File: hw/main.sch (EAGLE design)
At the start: 40 parts, among them Q1 732-MC14632.76KA-A0R, T1 863-MMBT4401LT1G, T2 863-MMBT4401LT1G, T3 863-MMBT4401LT1G, U1 579-MCP1703T-3002ECB, U2 638-CLS1522CL213RTR8, U3 595-MSP430G2553IPW28, U4 638-CLS1522CL213RTR8, X1 798-DF134P125H51, X2 798-DF134P125H51

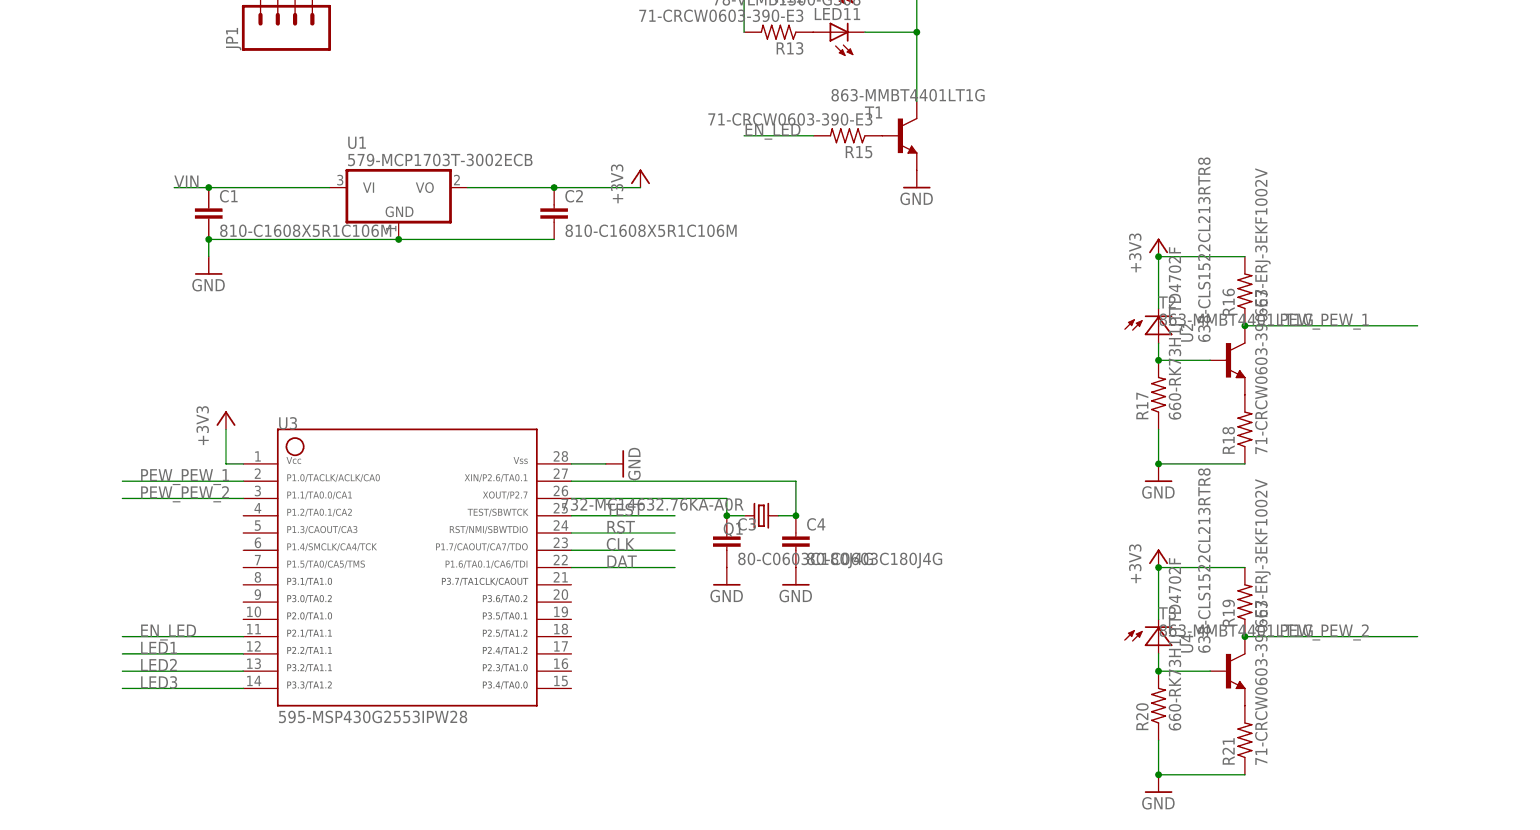
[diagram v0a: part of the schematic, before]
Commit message: Remove transistor and switch laser input to ADC polling.
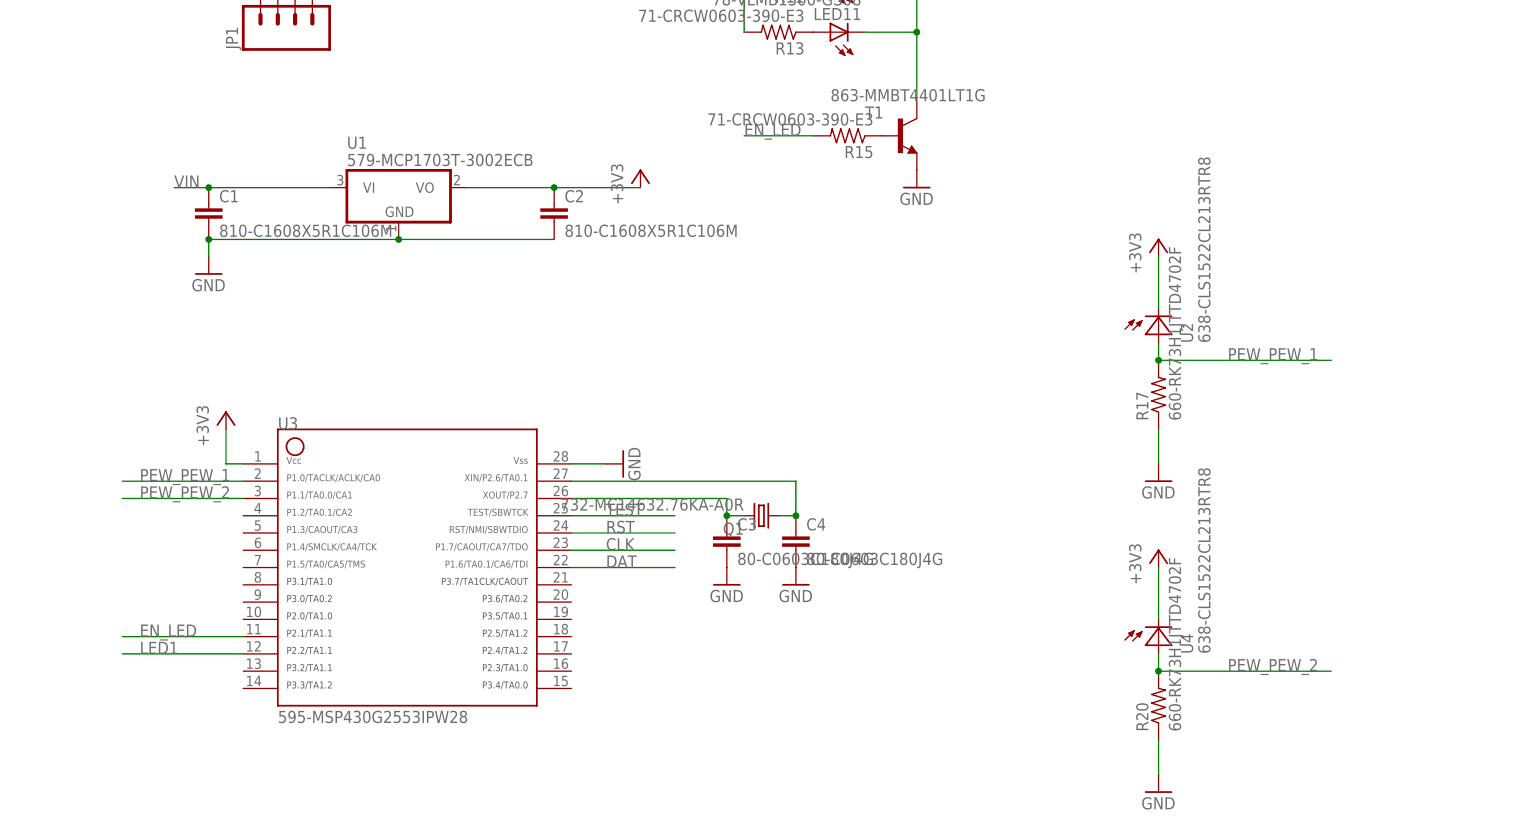
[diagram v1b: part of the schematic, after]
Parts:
- removed R16, R19: 667-ERJ-3EKF1002V, rcl:R-US_R0603
- removed R18, R21: 71-CRCW0603-390-E3, rcl:R-US_R0603
- removed T2, T3: 863-MMBT4401LT1G, transistor:MMBT4401LT1-NPN-SOT23-BEC
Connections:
- removed net 1: R20.2, T3.B, U4.A
- removed net 121231: R17.2, T2.B, U2.A
- removed net LED2: U3.13
- removed net LED3: U3.14
- removed net N$2: R18.2, T2.E
- removed net N$3: R21.2, T3.E
- net +3V3: no longer R16.2, R19.2
- net GND: no longer R18.1, R21.1
- net PEW_PEW_1: now also R17.2, U2.A; no longer R16.1, T2.C
- net PEW_PEW_2: now also R20.2, U4.A; no longer R19.1, T3.C
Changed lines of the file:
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@@
 <?xml version="1.0" encoding="utf-8"?>
 <!DOCTYPE eagle SYSTEM "eagle.dtd">
-<eagle version="6.0">
+<eagle version="6.1">
 <drawing>
 <settings>
@@
 <setting verticaltext="up"/>
 </settings>
-<grid distance="0.1" unitdist="inch" unit="inch" style="lines" multiple="1" display="no" altdistance="0.01" altunitdist="inch" altunit="inch"/>
+<grid distance="0.1" unitdist="inch" unit="inch" style="lines" multiple="1" display="yes" altdistance="0.01" altunitdist="inch" altunit="inch"/>
 <layers>
 <layer number="1" name="Top" color="4" fill="1" visible="no" active="no"/>
@@
 <part name="+3V3" library="supply1" deviceset="+3V3" device=""/>
 <part name="GND5" library="supply1" deviceset="GND" device=""/>
-<part name="T2" library="transistor" deviceset="*-NPN-" device="SOT23-BEC" technology="MMBT4401LT1" value="863-MMBT4401LT1G"/>
-<part name="R16" library="rcl" deviceset="R-US_" device="R0603" value="667-ERJ-3EKF1002V"/>
-<part name="R18" library="rcl" deviceset="R-US_" device="R0603" value="71-CRCW0603-390-E3"/>
 <part name="LED5" library="SparkFun-LED" deviceset="LED" device="0603" value="78-VLMB1300-GS08"/>
 <part name="LED3" library="SparkFun-LED" deviceset="LED" device="0603" value="78-VLMB1300-GS08"/>
@@
 <part name="+3V5" library="supply1" deviceset="+3V3" device=""/>
 <part name="GND6" library="supply1" deviceset="GND" device=""/>
-<part name="T3" library="transistor" deviceset="*-NPN-" device="SOT23-BEC" technology="MMBT4401LT1" value="863-MMBT4401LT1G"/>
-<part name="R19" library="rcl" deviceset="R-US_" device="R0603" value="667-ERJ-3EKF1002V"/>
-<part name="R21" library="rcl" deviceset="R-US_" device="R0603" value="71-CRCW0603-390-E3"/>
 <part name="LED11" library="SparkFun-LED" deviceset="LED" device="0603" value="78-VLMB1300-GS08"/>
 <part name="LED9" library="SparkFun-LED" deviceset="LED" device="0603" value="78-VLMB1300-GS08"/>
@@
 <instance part="+3V3" gate="G$1" x="142.24" y="71.12"/>
 <instance part="GND5" gate="1" x="142.24" y="35.56"/>
-<instance part="T2" gate="G$1" x="152.4" y="53.34"/>
-<instance part="R16" gate="G$1" x="154.94" y="63.5" rot="R90"/>
-<instance part="R18" gate="G$1" x="154.94" y="43.18" rot="R90"/>
 <instance part="LED5" gate="G$1" x="93.98" y="124.46" rot="R90"/>
 <instance part="LED3" gate="G$1" x="93.98" y="132.08" rot="R90"/>
@@
 <instance part="+3V5" gate="G$1" x="142.24" y="25.4"/>
 <instance part="GND6" gate="1" x="142.24" y="-10.16"/>
-<instance part="T3" gate="G$1" x="152.4" y="7.62"/>
-<instance part="R19" gate="G$1" x="154.94" y="17.78" rot="R90"/>
-<instance part="R21" gate="G$1" x="154.94" y="-2.54" rot="R90"/>
 <instance part="LED11" gate="G$1" x="93.98" y="101.6" rot="R90"/>
 <instance part="LED9" gate="G$1" x="93.98" y="109.22" rot="R90"/>
@@
 <pinref part="GND5" gate="1" pin="GND"/>
 <wire x1="142.24" y1="38.1" x2="142.24" y2="43.18" width="0.1524" layer="91"/>
-<pinref part="R18" gate="G$1" pin="1"/>
-<wire x1="142.24" y1="38.1" x2="154.94" y2="38.1" width="0.1524" layer="91"/>
-<junction x="142.24" y="38.1"/>
 </segment>
 <segment>
@@
 <pinref part="GND6" gate="1" pin="GND"/>
 <wire x1="142.24" y1="-7.62" x2="142.24" y2="-2.54" width="0.1524" layer="91"/>
-<pinref part="R21" gate="G$1" pin="1"/>
-<wire x1="142.24" y1="-7.62" x2="154.94" y2="-7.62" width="0.1524" layer="91"/>
-<junction x="142.24" y="-7.62"/>
 </segment>
 <segment>
@@
 </segment>
 </net>
-<net name="121231" class="0">
-<segment>
-<pinref part="U2" gate="G$1" pin="A"/>
-<pinref part="R17" gate="G$1" pin="2"/>
-<wire x1="142.24" y1="55.88" x2="142.24" y2="53.34" width="0.1524" layer="91"/>
-<wire x1="142.24" y1="53.34" x2="149.86" y2="53.34" width="0.1524" layer="91"/>
-<pinref part="T2" gate="G$1" pin="B"/>
-<junction x="142.24" y="53.34"/>
-</segment>
-</net>
 <net name="+3V3" class="0">
 <segment>
@@
 <wire x1="142.24" y1="60.96" x2="142.24" y2="68.58" width="0.1524" layer="91"/>
 <pinref part="+3V3" gate="G$1" pin="+3V3"/>
-<pinref part="R16" gate="G$1" pin="2"/>
-<wire x1="142.24" y1="68.58" x2="154.94" y2="68.58" width="0.1524" layer="91"/>
-<junction x="142.24" y="68.58"/>
 </segment>
 <segment>
@@
 <wire x1="142.24" y1="15.24" x2="142.24" y2="22.86" width="0.1524" layer="91"/>
 <pinref part="+3V5" gate="G$1" pin="+3V3"/>
-<pinref part="R19" gate="G$1" pin="2"/>
-<wire x1="142.24" y1="22.86" x2="154.94" y2="22.86" width="0.1524" layer="91"/>
-<junction x="142.24" y="22.86"/>
 </segment>
 <segment>
@@
 <net name="PEW_PEW_2" class="0">
 <segment>
-<pinref part="R19" gate="G$1" pin="1"/>
-<pinref part="T3" gate="G$1" pin="C"/>
-<wire x1="154.94" y1="12.7" x2="180.34" y2="12.7" width="0.1524" layer="91"/>
-<label x="160.02" y="12.7" size="1.778" layer="95"/>
-<junction x="154.94" y="12.7"/>
+<wire x1="142.24" y1="7.62" x2="167.64" y2="7.62" width="0.1524" layer="91"/>
+<label x="152.4" y="7.62" size="1.778" layer="95"/>
+<pinref part="U4" gate="G$1" pin="A"/>
+<pinref part="R20" gate="G$1" pin="2"/>
+<wire x1="142.24" y1="10.16" x2="142.24" y2="7.62" width="0.1524" layer="91"/>
+<junction x="142.24" y="7.62"/>
 </segment>
 <segment>
@@
 <wire x1="7.62" y1="33.02" x2="-10.16" y2="33.02" width="0.1524" layer="91"/>
 <label x="-7.62" y="33.02" size="1.778" layer="95"/>
-</segment>
-</net>
-<net name="N$2" class="0">
-<segment>
-<pinref part="T2" gate="G$1" pin="E"/>
-<pinref part="R18" gate="G$1" pin="2"/>
 </segment>
 </net>
@@
 <wire x1="256.54" y1="35.56" x2="238.76" y2="35.56" width="0.1524" layer="91"/>
 <label x="248.92" y="35.56" size="1.778" layer="95" rot="MR0"/>
-</segment>
-</net>
-<net name="1" class="0">
-<segment>
-<pinref part="U4" gate="G$1" pin="A"/>
-<pinref part="R20" gate="G$1" pin="2"/>
-<wire x1="142.24" y1="10.16" x2="142.24" y2="7.62" width="0.1524" layer="91"/>
-<wire x1="142.24" y1="7.62" x2="149.86" y2="7.62" width="0.1524" layer="91"/>
-<pinref part="T3" gate="G$1" pin="B"/>
-<junction x="142.24" y="7.62"/>
-</segment>
-</net>
-<net name="N$3" class="0">
-<segment>
-<pinref part="T3" gate="G$1" pin="E"/>
-<pinref part="R21" gate="G$1" pin="2"/>
 </segment>
 </net>
@@
 <net name="PEW_PEW_1" class="0">
 <segment>
-<pinref part="R16" gate="G$1" pin="1"/>
-<pinref part="T2" gate="G$1" pin="C"/>
-<wire x1="154.94" y1="58.42" x2="180.34" y2="58.42" width="0.1524" layer="91"/>
-<label x="160.02" y="58.42" size="1.778" layer="95"/>
-<junction x="154.94" y="58.42"/>
-</segment>
-<segment>
 <pinref part="U3" gate="G$1" pin="2"/>
 <wire x1="7.62" y1="35.56" x2="-10.16" y2="35.56" width="0.1524" layer="91"/>
 <label x="-7.62" y="35.56" size="1.778" layer="95"/>
+</segment>
+<segment>
+<pinref part="U2" gate="G$1" pin="A"/>
+<pinref part="R17" gate="G$1" pin="2"/>
+<wire x1="142.24" y1="55.88" x2="142.24" y2="53.34" width="0.1524" layer="91"/>
+<wire x1="142.24" y1="53.34" x2="167.64" y2="53.34" width="0.1524" layer="91"/>
+<junction x="142.24" y="53.34"/>
+<label x="152.4" y="53.34" size="1.778" layer="95"/>
 </segment>
 </net>
@@
 </segment>
 </net>
-<net name="LED2" class="0">
-<segment>
-<pinref part="U3" gate="G$1" pin="13"/>
-<wire x1="7.62" y1="7.62" x2="-10.16" y2="7.62" width="0.1524" layer="91"/>
-<label x="-7.62" y="7.62" size="1.778" layer="95"/>
-</segment>
-</net>
-<net name="LED3" class="0">
-<segment>
-<pinref part="U3" gate="G$1" pin="14"/>
-<wire x1="7.62" y1="5.08" x2="-10.16" y2="5.08" width="0.1524" layer="91"/>
-<label x="-7.62" y="5.08" size="1.778" layer="95"/>
-</segment>
-</net>

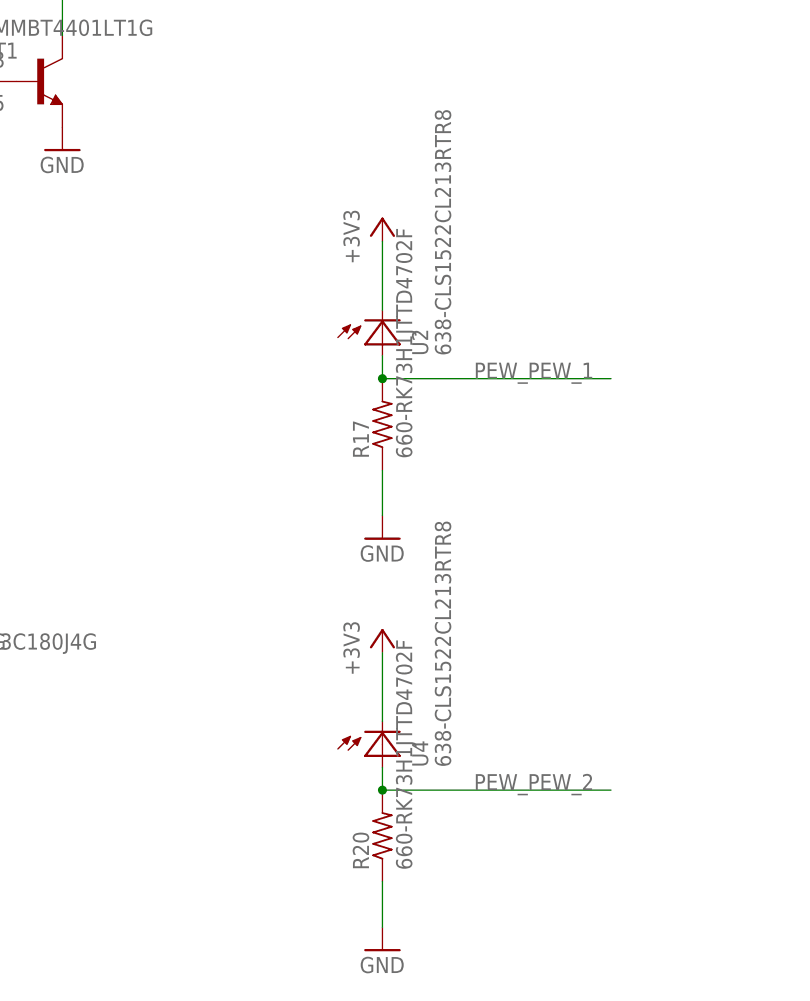
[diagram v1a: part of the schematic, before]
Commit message: Fix resistor value for light detector.
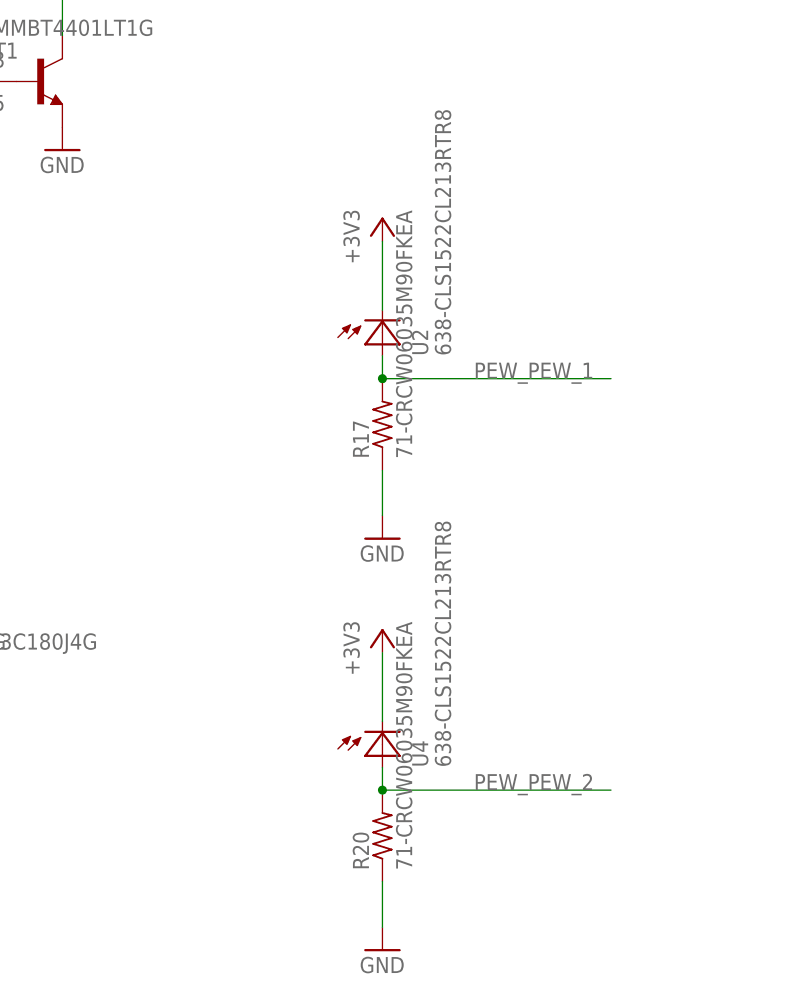
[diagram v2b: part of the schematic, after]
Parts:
- R17, R20: value 660-RK73H1JTTD4702F -> 71-CRCW06035M90FKEA
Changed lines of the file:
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@@
 <setting verticaltext="up"/>
 </settings>
-<grid distance="0.1" unitdist="inch" unit="inch" style="lines" multiple="1" display="yes" altdistance="0.01" altunitdist="inch" altunit="inch"/>
+<grid distance="0.1" unitdist="inch" unit="inch" style="lines" multiple="1" display="no" altdistance="0.01" altunitdist="inch" altunit="inch"/>
 <layers>
 <layer number="1" name="Top" color="4" fill="1" visible="no" active="no"/>
@@
 <part name="GND3" library="supply1" deviceset="GND" device=""/>
 <part name="GND4" library="supply1" deviceset="GND" device=""/>
-<part name="R17" library="rcl" deviceset="R-US_" device="R0603" value="660-RK73H1JTTD4702F"/>
+<part name="R17" library="rcl" deviceset="R-US_" device="R0603" value="71-CRCW06035M90FKEA"/>
 <part name="U1" library="linear" deviceset="MCP1703" device="CB" value="579-MCP1703T-3002ECB"/>
 <part name="+3V1" library="supply1" deviceset="+3V3" device=""/>
@@
 <part name="X1" library="con-molex" deviceset="53?-04" device="261" value="798-DF134P125H51"/>
 <part name="U4" library="torpedo" deviceset="CLS15" device="CLS15" value="638-CLS1522CL213RTR8"/>
-<part name="R20" library="rcl" deviceset="R-US_" device="R0603" value="660-RK73H1JTTD4702F"/>
+<part name="R20" library="rcl" deviceset="R-US_" device="R0603" value="71-CRCW06035M90FKEA"/>
 <part name="+3V5" library="supply1" deviceset="+3V3" device=""/>
 <part name="GND6" library="supply1" deviceset="GND" device=""/>

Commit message: Updated target to simplify circuit and make immune to spurious light sources.
The design has been reduced in size from ~40mm diameter to ~21mm diameter. The sensor was changed from a single-color (red) detector to a full-spectrum + white sensor since the old version would get tripped by white light (and camera flashes). The microcontroller was changed from the MSP430G2553 to the MSP430G2452 in the 14 pin package to save space. The new target will mount from the bottom and sit in the bottom of the table tennis ball instead of in the middle.
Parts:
- removed C3, C4: 80-C0603C180J4G, SparkFun-Passives:CAP0603-CAP
- removed LED1, LED11, LED3, LED5, LED7, LED9: 78-VLMB1300-GS08, SparkFun-LED:LED0603
- removed LED2, LED4: 720-LGQ971-KN-1, SparkFun-LED:LED0603
- removed Q1: 732-MC14632.76KA-A0R, SparkFun:CRYSTALEPSONMC146
- removed R11, R13, R15, R9: 71-CRCW0603-390-E3, rcl:R-US_R0603
- removed R17, R20: 71-CRCW06035M90FKEA, rcl:R-US_R0603
- removed U4: 638-CLS1522CL213RTR8, torpedo:CLS15CLS15
- added D1, D2: VLMB1300-GS08, SparkFun-LED:LED0603
- added D3, D4: VLMS1300-GS08, SparkFun-LED:LED0603
- added R8: CRCW0603200RFKEA, rcl:R-US_R0603
- added T2: PMBT4401,215, transistor:MMBT4401LT1-NPN-SOT23-BEC
- C1, C2: value 810-C1608X5R1C106M -> C1608X5R1C106M080AB
- JP1: device SparkFun:M04PTH -> SparkFun-Connectors:M03PTH
- R1, R2: value 71-CRCW0603-390-E3 -> RK73H1JTTD4702F
- R3, R6: value 660-RK73H1JTTD4702F -> CRCW0603200RFKEA
- R4, R5, R7: value 71-CRCW0603-390-E3 -> CRCW0603200RFKEA
- T1: value 863-MMBT4401LT1G -> PMBT4401,215
- U1: value 579-MCP1703T-3002ECB -> MCP1703T-3002E/CB
- U2: value 638-CLS1522CL213RTR8 -> MSP430G2452IPW14R; device torpedo:CLS15CLS15 -> TI_MSP430_v16:G2X[1/5]2---PW14
- U3: value 595-MSP430G2553IPW28 -> TCS3414CS; device torpedo:MSP430G2553 -> torpedo:TCS3414CS
- X1, X2: value 798-DF134P125H51 -> DF13-4P-1.25V(50); device con-molex:53261-04 -> con-molex:53398-04
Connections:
- removed net EN_LED: R15.2, U3.11
- removed net LED1: LED2.C, LED4.C, U3.12
- removed net N$11: LED7.A, R9.1
- removed net N$12: C4.1, Q1.1, U3.27
- removed net N$13: C3.1, Q1.2, U3.26
- removed net N$5: LED1.A, R1.1
- removed net N$9: LED4.A, R5.1
- removed net PEW_PEW_1: R17.2, U2.A, U3.2
- removed net PEW_PEW_2: R20.2, U3.3, U4.A
- new net BLUE_LED: R5.2, U2.5
- new net CNT: U2.2, X1-4.S, X2-4.S
- new net INT: U2.7, U3.INT
- new net N$2: D3.C, D4.C, T2.C
- new net RED_LED: R8.2, U2.4
- new net SET: U2.3, X1-3.S, X2-3.S
- new net SYNC: U2.6, U3.SYNC
- net +3V3: now also R6.2, U2.1, U3.VCC; no longer JP1.4, R11.2, R13.2, R2.2, R5.2, R9.2, U2.C, U3.1, U4.C
- net CLK: now also U2.8, U3.SCL; no longer U3.23, X1-3.S, X2-3.S
- net DAT: now also U2.9, U3.SDA; no longer U3.22, X1-4.S, X2-4.S
- net GND: now also R2.1, T2.E, U2.14, U3.GND; no longer C3.2, C4.2, R17.1, R20.1, R6.1, U3.28
- net LED: now also D1.C, D2.C; no longer LED1.C, LED11.C, LED3.C, LED5.C, LED7.C, LED9.C
- net N$1: now also D4.A; no longer LED5.A
- net N$10: now also D3.A, R6.1; no longer LED2.A, R2.1
- net N$18: now also R5.1; no longer R15.1
- net N$4: now also R8.1, T2.B; no longer LED3.A, R4.1
- net N$6: now also D2.A, R4.1; no longer LED11.A, R13.1
- net N$7: now also D1.A, R3.1; no longer LED9.A, R11.1
- net RST: now also JP1.2, R2.2, U2.10; no longer JP1.1, R3.1, U3.24
- net TEST: now also JP1.1, R1.1, U2.11; no longer JP1.2, R6.2, U3.25
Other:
- note added: "Programming Connector"
- moved on the sheet: C1, C2, R1, R2, R3, R4, R5, R6, R7, T1, U1, X1-1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
